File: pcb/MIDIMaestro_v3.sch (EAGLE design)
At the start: 38 parts, among them IC1 74LS133N, IC3 74LS138N, IC4 68B50, IC5 74LS04N, IC6 74*161, X1 MIDI_IN, X2 MIDI_THRU, X3 MIDI_OUT, X4 EXPANSION_PORT_COCO

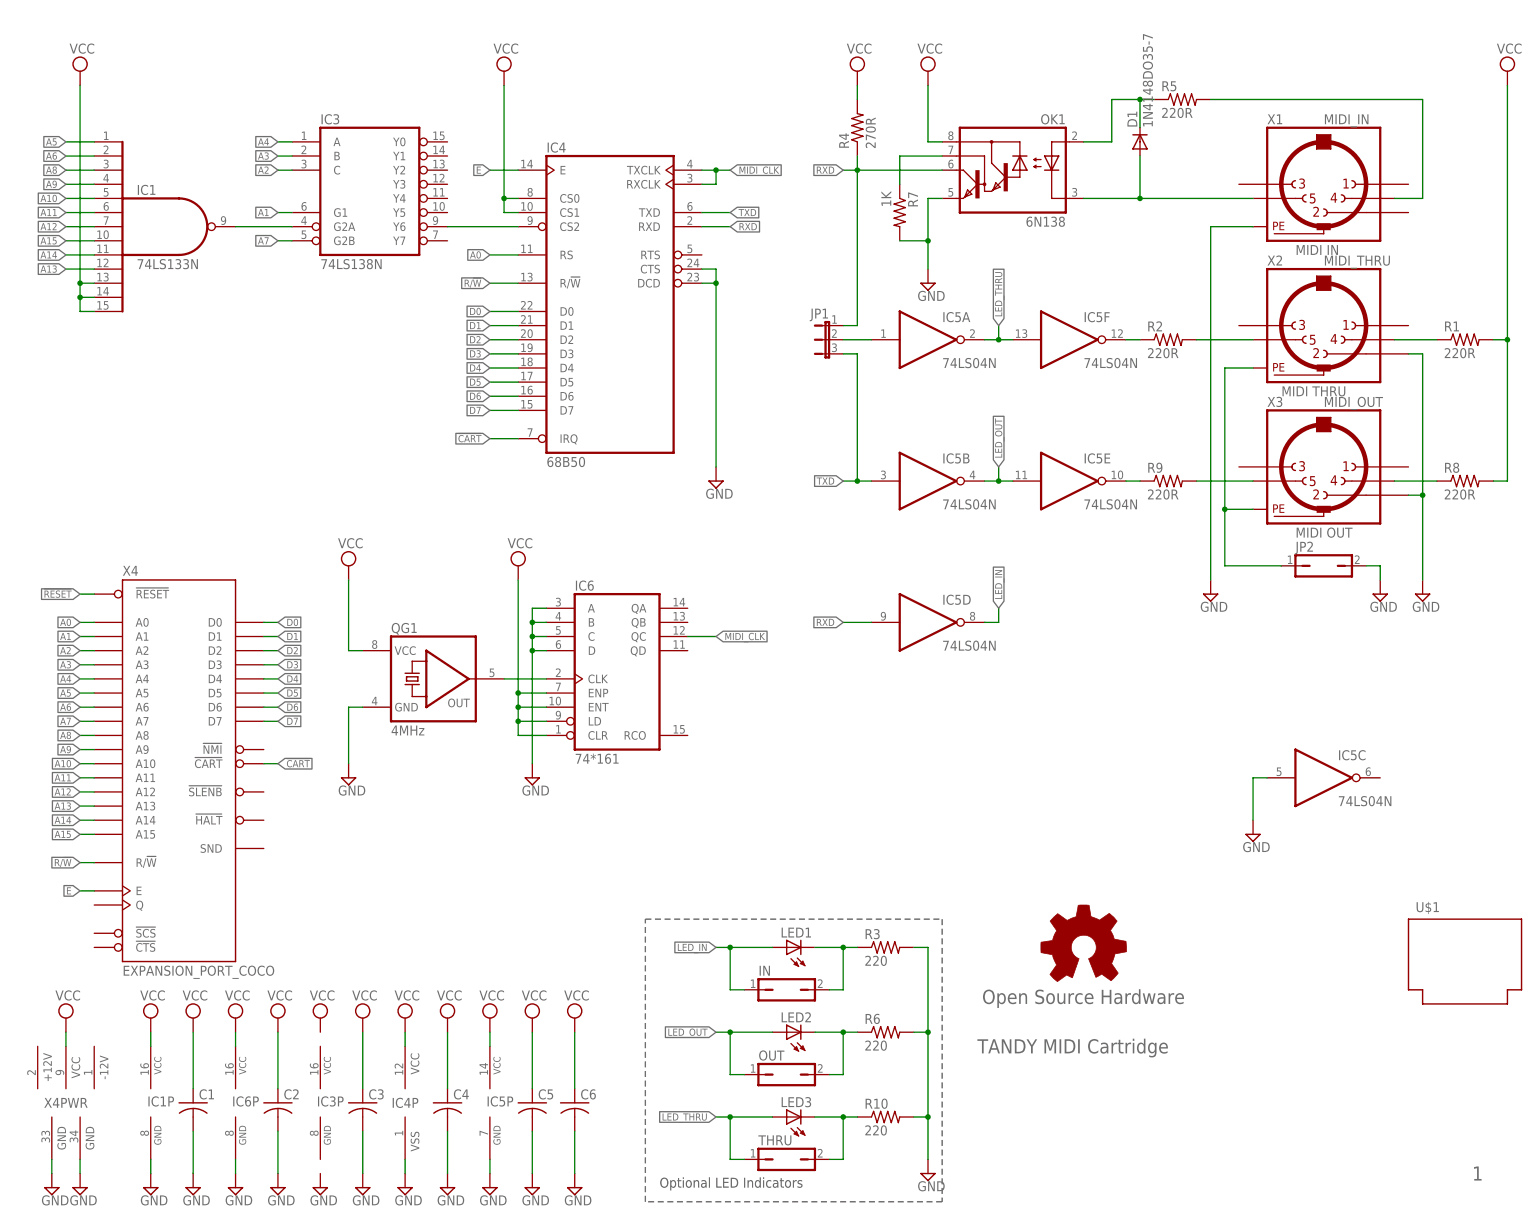
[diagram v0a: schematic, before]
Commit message: Changed name, Added Dragon variant
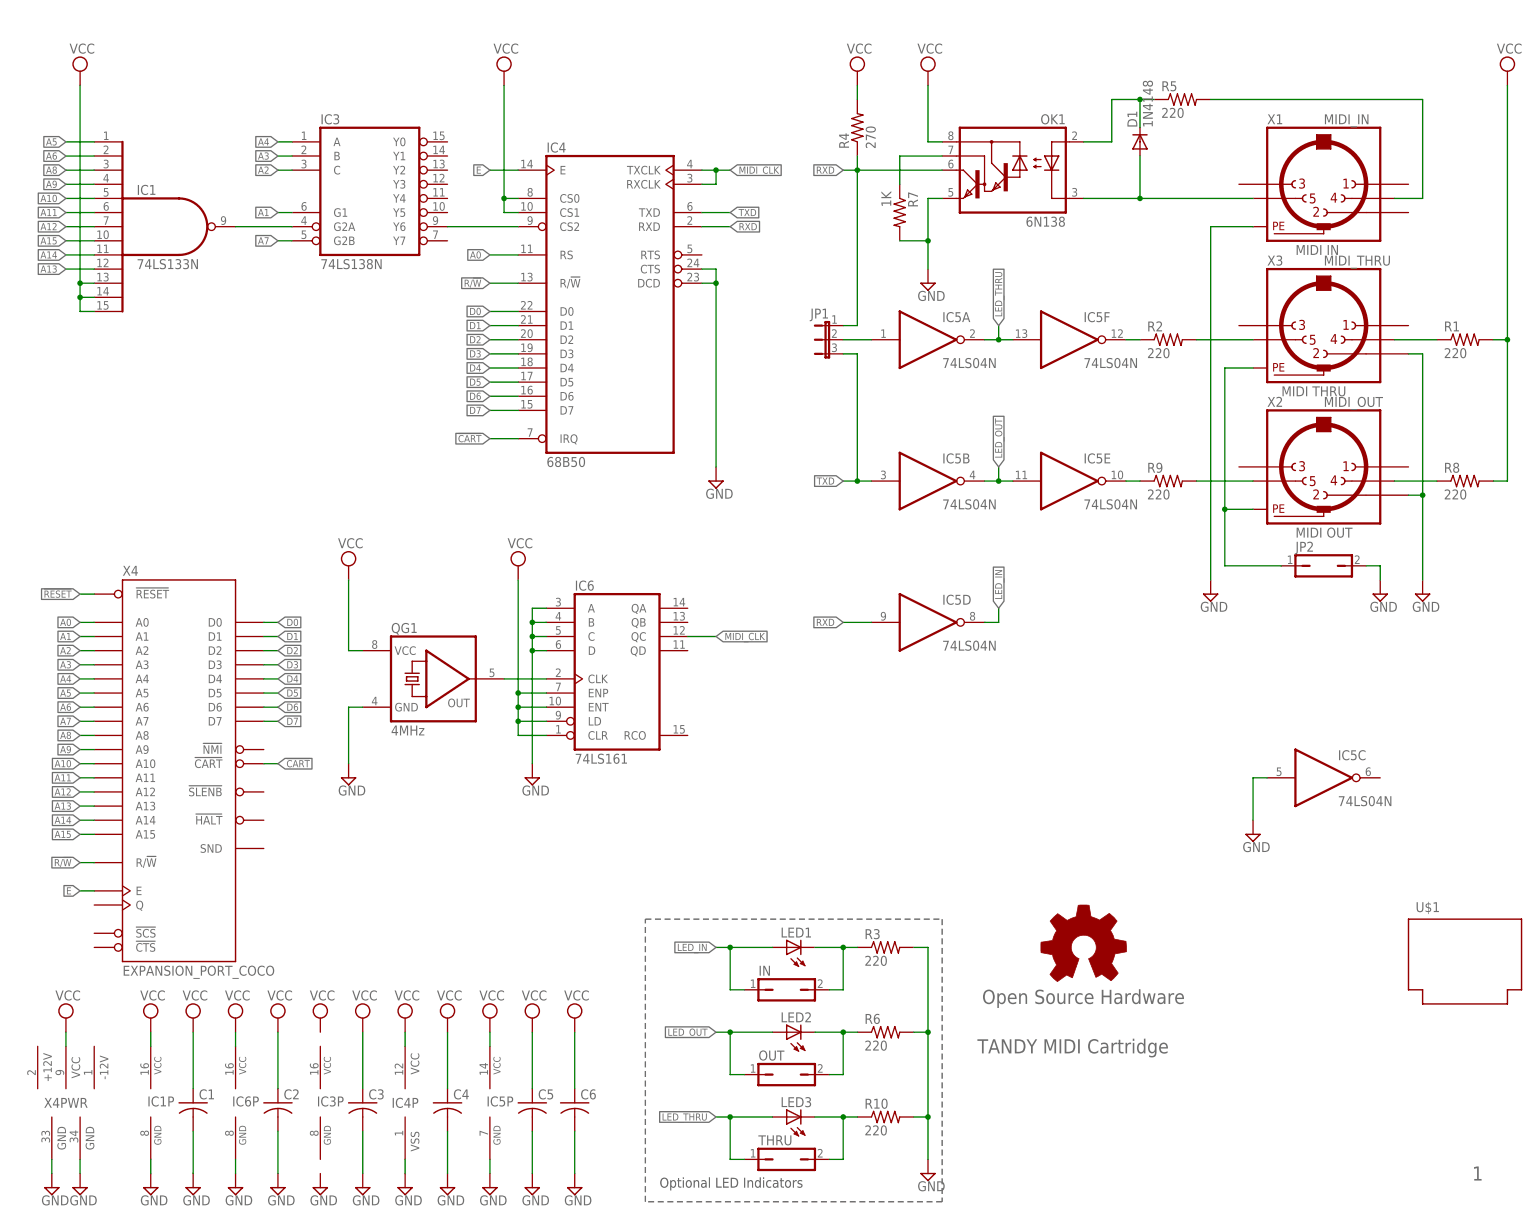
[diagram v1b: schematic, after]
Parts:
- D1: value 1N4148DO35-7 -> 1N4148
- IC6: value 74*161 -> 74LS161
- R1, R2, R5, R8, R9: value 220R -> 220
- R4: value 270R -> 270
- X2: value MIDI_THRU -> MIDI_OUT
- X3: value MIDI_OUT -> MIDI_THRU
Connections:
- net N$1: now also X2.5; no longer X3.5
- net N$10: now also X3.5; no longer X2.5
- net N$13: now also X3.4; no longer X2.4
- net N$3: now also X2.4; no longer X3.4
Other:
- moved on the sheet: X2, X3
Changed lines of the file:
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@@
 </classes>
 <parts>
-<part name="R8" library="resistor" deviceset="R-US_" device="0204/7" value="220R"/>
-<part name="R9" library="resistor" deviceset="R-US_" device="0204/7" value="220R"/>
-<part name="R5" library="resistor" deviceset="R-US_" device="0204/7" value="220R"/>
-<part name="R2" library="resistor" deviceset="R-US_" device="0204/7" value="220R"/>
+<part name="R8" library="resistor" deviceset="R-US_" device="0204/7" value="220"/>
+<part name="R9" library="resistor" deviceset="R-US_" device="0204/7" value="220"/>
+<part name="R5" library="resistor" deviceset="R-US_" device="0204/7" value="220"/>
+<part name="R2" library="resistor" deviceset="R-US_" device="0204/7" value="220"/>
 <part name="SUPPLY2" library="supply2" deviceset="GND" device=""/>
-<part name="R1" library="resistor" deviceset="R-US_" device="0204/7" value="220R"/>
+<part name="R1" library="resistor" deviceset="R-US_" device="0204/7" value="220"/>
 <part name="R7" library="resistor" deviceset="R-US_" device="0204/7" value="1K"/>
 <part name="SUPPLY11" library="supply2" deviceset="GND" device=""/>
-<part name="R4" library="resistor" deviceset="R-US_" device="0204/7" value="270R"/>
+<part name="R4" library="resistor" deviceset="R-US_" device="0204/7" value="270"/>
 <part name="V2" library="supply2" deviceset="VCC" device=""/>
 <part name="V5" library="supply2" deviceset="VCC" device=""/>
@@
 <part name="IC3" library="74xx-us-jlb" deviceset="74*138" device="N" technology="LS"/>
 <part name="X1" library="con-hirschmann" deviceset="MAB5SH" device="" value="MIDI_IN"/>
-<part name="X2" library="con-hirschmann" deviceset="MAB5SH" device="" value="MIDI_THRU"/>
-<part name="X3" library="con-hirschmann" deviceset="MAB5SH" device="" value="MIDI_OUT"/>
+<part name="X3" library="con-hirschmann" deviceset="MAB5SH" device="" value="MIDI_THRU"/>
+<part name="X2" library="con-hirschmann" deviceset="MAB5SH" device="" value="MIDI_OUT"/>
 <part name="IC4" library="micro-motorola" deviceset="6850" device="-RP" value="68B50"/>
 <part name="V3" library="supply2" deviceset="VCC" device=""/>
@@
 <part name="SUPPLY28" library="supply2" deviceset="GND" device=""/>
 <part name="SUPPLY29" library="supply2" deviceset="GND" device=""/>
-<part name="IC6" library="74xx-us-jlb" deviceset="74*160" device="N" value="74*161"/>
+<part name="IC6" library="74xx-us-jlb" deviceset="74*160" device="N" value="74LS161"/>
 <part name="V4" library="supply2" deviceset="VCC" device=""/>
-<part name="D1" library="diode-jlb" deviceset="1N4148" device="DO35-7"/>
+<part name="D1" library="diode-jlb" deviceset="1N4148" device="DO35-7" value="1N4148"/>
 <part name="QG1" library="crystal" deviceset="QG5460" device="" value="4MHz"/>
 <part name="V6" library="supply2" deviceset="VCC" device=""/>
@@
 <instance part="IC3" gate="A" x="68.58" y="185.42"/>
 <instance part="X1" gate="G$1" x="238.76" y="185.42"/>
-<instance part="X2" gate="G$1" x="238.76" y="160.02"/>
-<instance part="X3" gate="G$1" x="238.76" y="134.62"/>
+<instance part="X3" gate="G$1" x="238.76" y="160.02"/>
+<instance part="X2" gate="G$1" x="238.76" y="134.62"/>
 <instance part="IC4" gate="A" x="109.22" y="170.18"/>
 <instance part="V3" gate="G$1" x="91.44" y="205.74"/>
@@
 <pinref part="SUPPLY2" gate="GND" pin="GND"/>
 <wire x1="256.54" y1="129.54" x2="256.54" y2="114.3" width="0.1524" layer="91"/>
-<pinref part="X3" gate="G$1" pin="2"/>
+<pinref part="X2" gate="G$1" pin="2"/>
 <wire x1="254" y1="129.54" x2="256.54" y2="129.54" width="0.1524" layer="91"/>
 <junction x="256.54" y="129.54"/>
 <wire x1="256.54" y1="154.94" x2="256.54" y2="129.54" width="0.1524" layer="91"/>
 <wire x1="254" y1="154.94" x2="256.54" y2="154.94" width="0.1524" layer="91"/>
-<pinref part="X2" gate="G$1" pin="2"/>
+<pinref part="X3" gate="G$1" pin="2"/>
 </segment>
 <segment>
@@
 <wire x1="226.06" y1="132.08" x2="215.9" y2="132.08" width="0.1524" layer="91"/>
 <pinref part="R9" gate="G$1" pin="2"/>
-<pinref part="X3" gate="G$1" pin="5"/>
+<pinref part="X2" gate="G$1" pin="5"/>
 </segment>
 </net>
@@
 <wire x1="215.9" y1="157.48" x2="226.06" y2="157.48" width="0.1524" layer="91"/>
 <pinref part="R2" gate="G$1" pin="2"/>
-<pinref part="X2" gate="G$1" pin="5"/>
+<pinref part="X3" gate="G$1" pin="5"/>
 </segment>
 </net>
@@
 <wire x1="251.46" y1="157.48" x2="259.08" y2="157.48" width="0.1524" layer="91"/>
 <pinref part="R1" gate="G$1" pin="1"/>
-<pinref part="X2" gate="G$1" pin="4"/>
+<pinref part="X3" gate="G$1" pin="4"/>
 </segment>
 </net>
@@
 <wire x1="251.46" y1="132.08" x2="259.08" y2="132.08" width="0.1524" layer="91"/>
 <pinref part="R8" gate="G$1" pin="1"/>
-<pinref part="X3" gate="G$1" pin="4"/>
+<pinref part="X2" gate="G$1" pin="4"/>
 </segment>
 </net>
@@
 <net name="N$2" class="0">
 <segment>
+<pinref part="X3" gate="G$1" pin="PE"/>
+<wire x1="226.06" y1="152.4" x2="220.98" y2="152.4" width="0.1524" layer="91"/>
 <pinref part="X2" gate="G$1" pin="PE"/>
-<wire x1="226.06" y1="152.4" x2="220.98" y2="152.4" width="0.1524" layer="91"/>
-<pinref part="X3" gate="G$1" pin="PE"/>
 <wire x1="220.98" y1="127" x2="226.06" y2="127" width="0.1524" layer="91"/>
 <wire x1="220.98" y1="127" x2="220.98" y2="116.84" width="0.1524" layer="91"/>
